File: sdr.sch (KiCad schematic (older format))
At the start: 0 parts

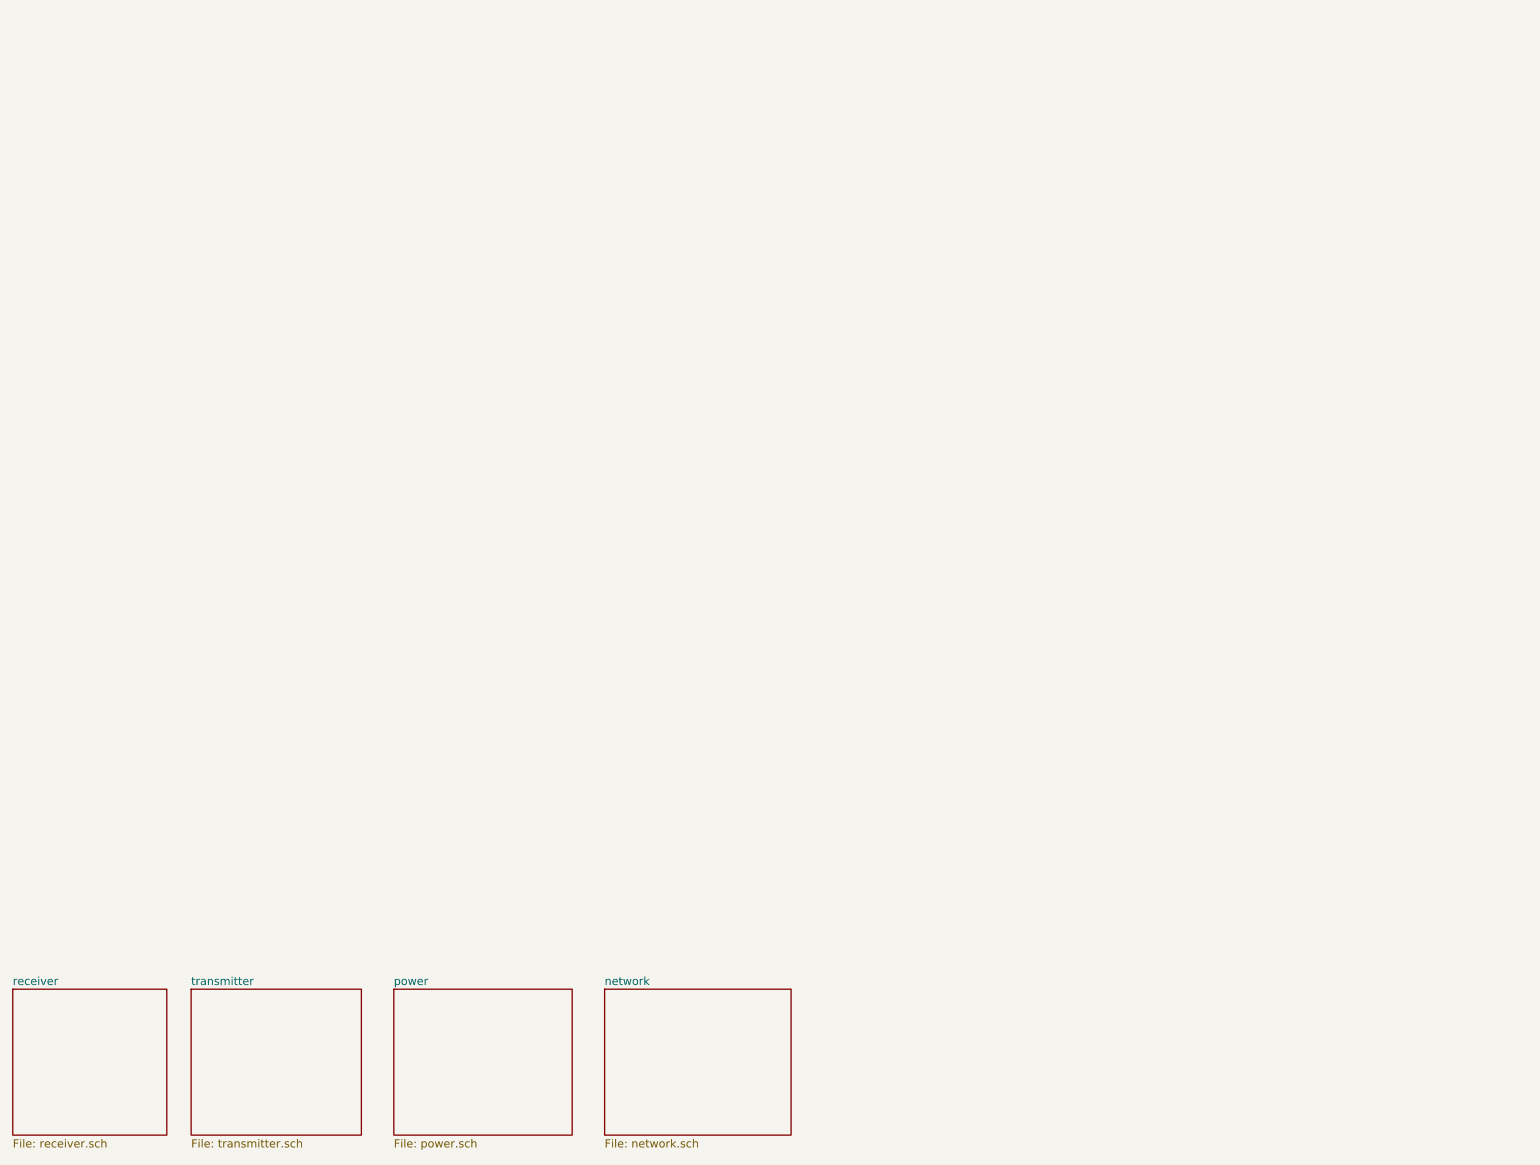
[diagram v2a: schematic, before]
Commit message: work on fpga connections
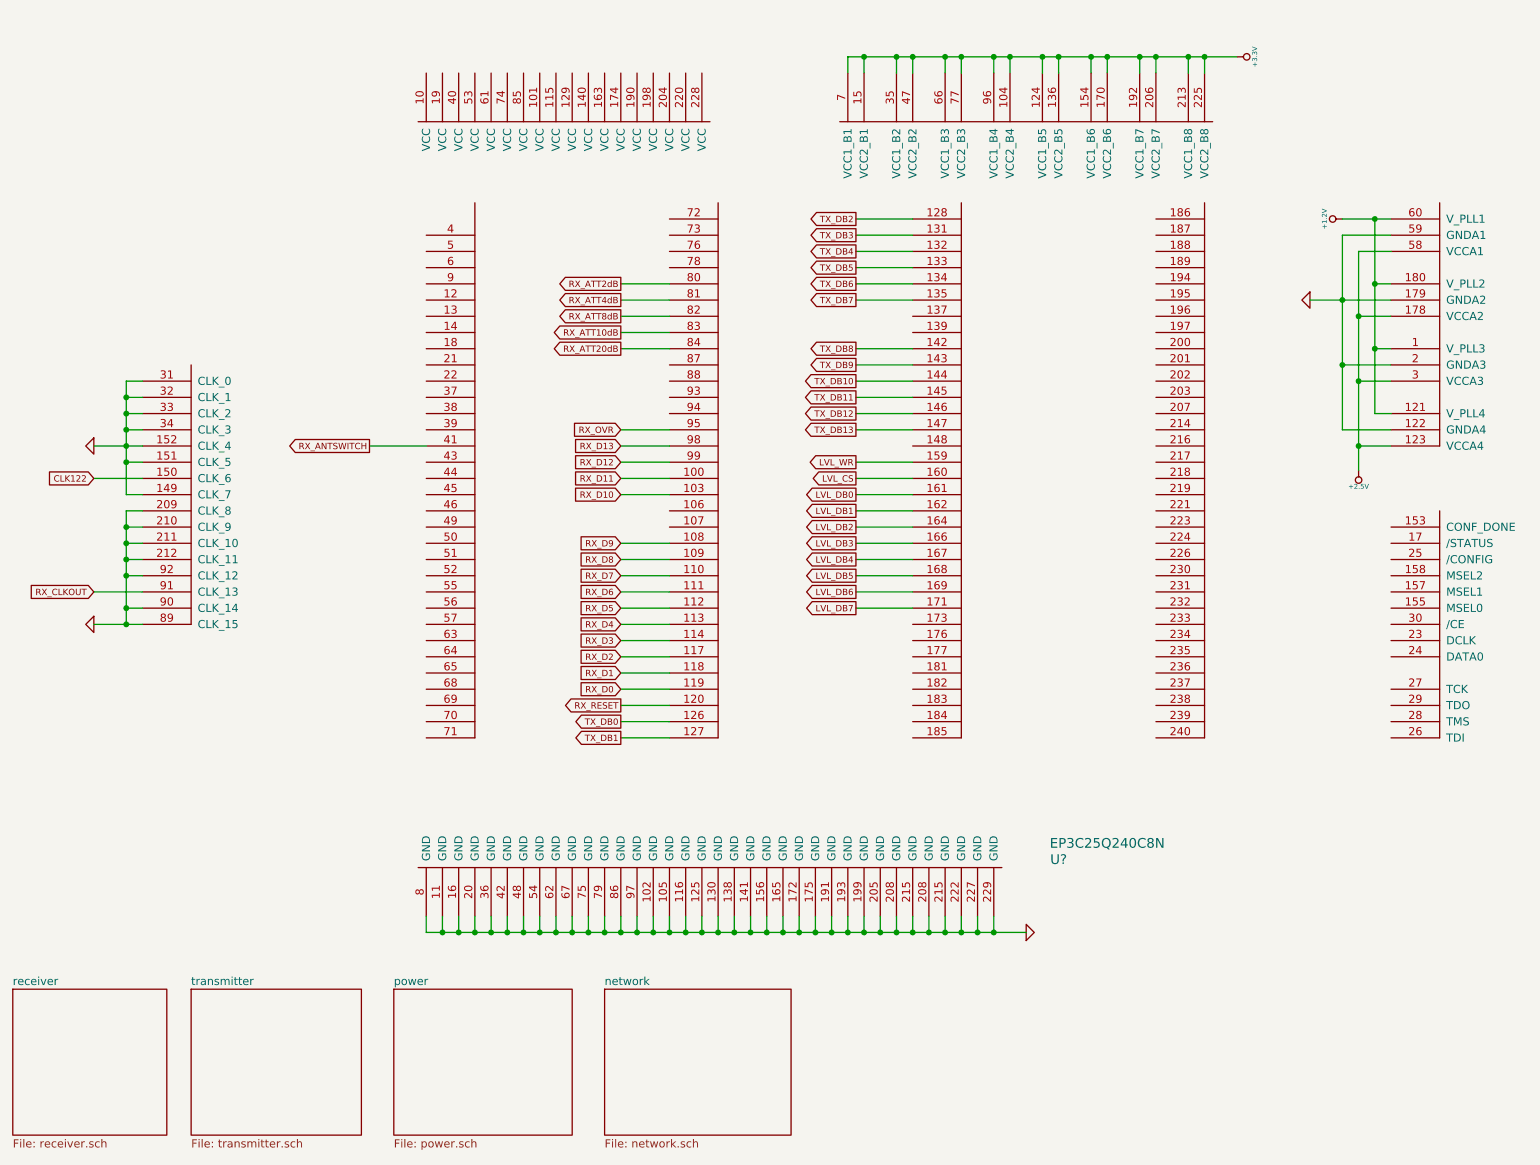
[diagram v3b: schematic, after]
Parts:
- added U?: EP3C25Q240C8N, symbol EP3C25Q240C8N
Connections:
- new net +1.2V: U?.1 (V_PLL3), U?.121 (V_PLL4), U?.180 (V_PLL2), U?.60 (V_PLL1)
- new net +2.5V: U?.123 (VCCA4), U?.178 (VCCA2), U?.3 (VCCA3), U?.58 (VCCA1)
- new net +3.3V: U?.104 (VCC2_B4), U?.124 (VCC1_B5), U?.136 (VCC2_B5), U?.15 (VCC2_B1), U?.154 (VCC1_B6), U?.170 (VCC2_B6), U?.192 (VCC1_B7), U?.206 (VCC2_B7), U?.213 (VCC1_B8), U?.225 (VCC2_B8), U?.35 (VCC1_B2), U?.47 (VCC2_B2), U?.66 (VCC1_B3), U?.7 (VCC1_B1), U?.77 (VCC2_B3), U?.96 (VCC1_B4)
- new net CLK122: U?.150 (CLK_6)
- new net GND: U?.102 (GND), U?.105 (GND), U?.11 (GND), U?.116 (GND), U?.122 (GNDA4), U?.125 (GND), U?.130 (GND), U?.138 (GND), U?.141 (GND), U?.149 (CLK_7), U?.151 (CLK_5), U?.152 (CLK_4), U?.156 (GND), U?.16 (GND), U?.165 (GND), U?.172 (GND), U?.175 (GND), U?.179 (GNDA2), U?.191 (GND), U?.193 (GND), U?.199 (GND), U?.2 (GNDA3), U?.20 (GND), U?.205 (GND), U?.208 (GND), U?.209 (CLK_8), U?.210 (CLK_9), U?.211 (CLK_10), U?.212 (CLK_11), U?.215 (GND), U?.222 (GND), U?.227 (GND), U?.229 (GND), U?.31 (CLK_0), U?.32 (CLK_1), U?.33 (CLK_2), U?.34 (CLK_3), U?.36 (GND), U?.42 (GND), U?.48 (GND), U?.54 (GND), U?.59 (GNDA1), U?.62 (GND), U?.67 (GND), U?.75 (GND), U?.79 (GND), U?.8 (GND), U?.86 (GND), U?.89 (CLK_15), U?.90 (CLK_14), U?.92 (CLK_12), U?.97 (GND)
- new net LVL_CS: U?.160
- new net LVL_DB0: U?.161
- new net LVL_DB1: U?.162
- new net LVL_DB2: U?.164
- new net LVL_DB3: U?.166
- new net LVL_DB4: U?.167
- new net LVL_DB5: U?.168
- new net LVL_DB6: U?.169
- new net LVL_DB7: U?.171
- new net LVL_WR: U?.159
- new net RX_ANTSWITCH: U?.41
- new net RX_ATT10dB: U?.83
- new net RX_ATT20dB: U?.84
- new net RX_ATT2dB: U?.80
- new net RX_ATT4dB: U?.81
- new net RX_ATT8dB: U?.82
- new net RX_CLKOUT: U?.91 (CLK_13)
- new net RX_D0: U?.119
- new net RX_D1: U?.118
- new net RX_D10: U?.103
- new net RX_D11: U?.100
- new net RX_D12: U?.99
- new net RX_D13: U?.98
- new net RX_D2: U?.117
- new net RX_D3: U?.114
- new net RX_D4: U?.113
- new net RX_D5: U?.112
- new net RX_D6: U?.111
- new net RX_D7: U?.110
- new net RX_D8: U?.109
- new net RX_D9: U?.108
- new net RX_OVR: U?.95
- new net RX_RESET: U?.120
- new net TX_DB0: U?.126
- new net TX_DB1: U?.127
- new net TX_DB10: U?.144
- new net TX_DB11: U?.145
- new net TX_DB12: U?.146
- new net TX_DB13: U?.147
- new net TX_DB2: U?.128
- new net TX_DB3: U?.131
- new net TX_DB4: U?.132
- new net TX_DB5: U?.133
- new net TX_DB6: U?.134
- new net TX_DB7: U?.135
- new net TX_DB8: U?.142
- new net TX_DB9: U?.143

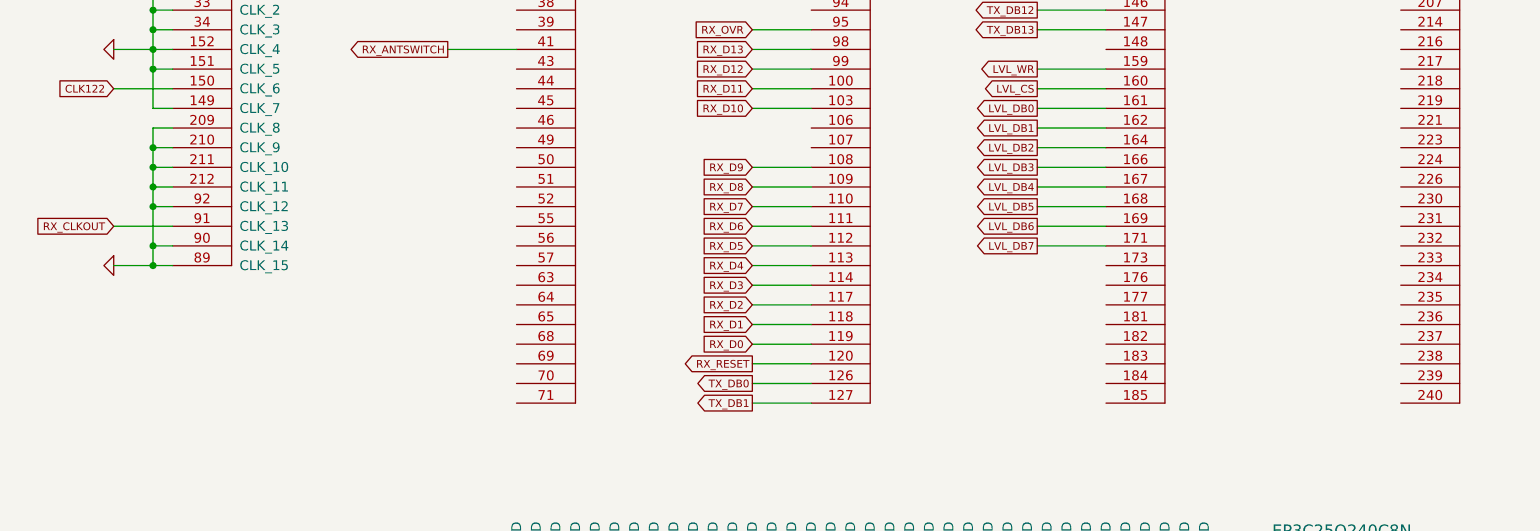
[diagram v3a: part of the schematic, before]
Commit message: some work on the network section
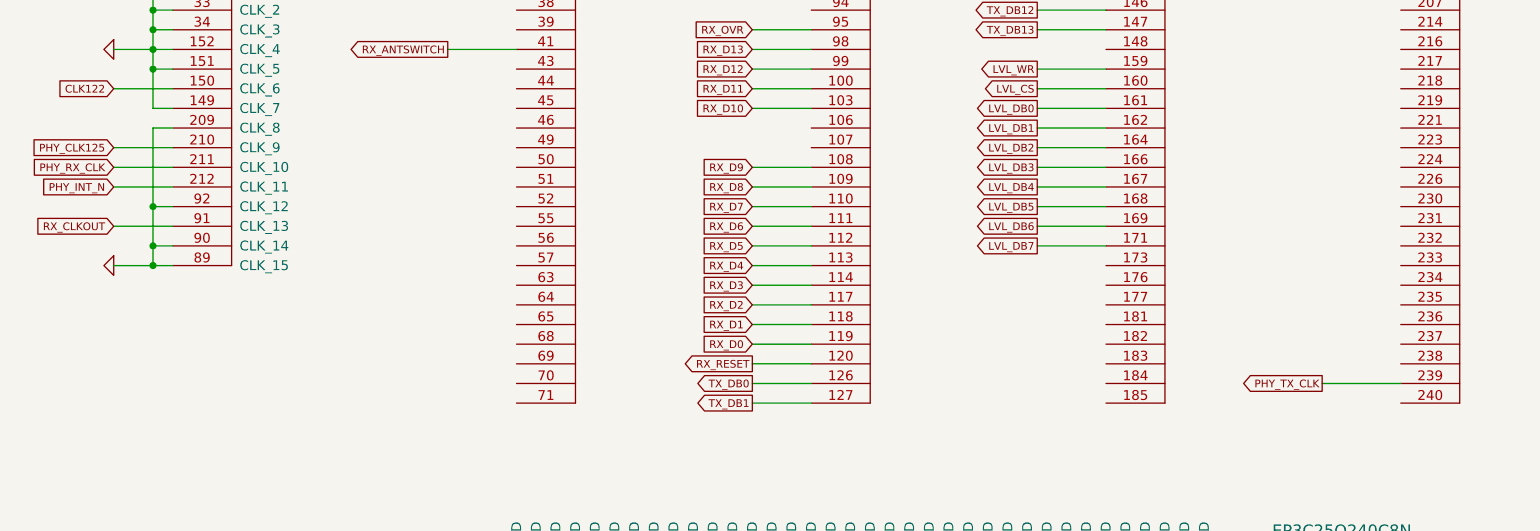
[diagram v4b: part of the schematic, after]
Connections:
- net GND: no longer U?.210 (CLK_9), U?.211 (CLK_10), U?.212 (CLK_11)
- net PHY_TX_CLK: now reaches U?.239
- new net PHY_CLK125: U?.210 (CLK_9)
- new net PHY_INT_N: U?.212 (CLK_11)
- new net PHY_RX_CLK: U?.211 (CLK_10)

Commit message: additions and fixes
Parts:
- added R?: R, symbol R
- added U?: EPCS16, symbol EPCS16
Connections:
- net +1.2V: now also U?.10 (VCC), U?.101 (VCC), U?.115 (VCC), U?.129 (VCC), U?.140 (VCC), U?.163 (VCC), U?.174 (VCC), U?.19 (VCC), U?.190 (VCC), U?.198 (VCC), U?.204 (VCC), U?.220 (VCC), U?.228 (VCC), U?.40 (VCC), U?.53 (VCC), U?.61 (VCC), U?.74 (VCC), U?.85 (VCC)
- net +3.3V: now also U?.157 (MSEL1), U?.3 (VCC), U?.7 (VCC), U?.8 (VCC)
- net GND: now also U?.155 (MSEL0), U?.158 (MSEL2), U?.~ (GND)
- net ASDI: now reaches U?.12
- net ASDI: now also U?.5 (ASDI)
- net NCS: now reaches U?.14
- net NCS: now also U?.1 (NCS)
- net at U?.23 (DCLK): now also U?.6 (DCLK)
- net at U?.24 (DATA0): now also R?.1
- new net: R?.2, U?.2 (DATA)
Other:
- note added: "Main FPGA"

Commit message: fixes
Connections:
- net GND: no longer U?.209 (CLK_8)
- new net CLK_25MHZ: U?.209 (CLK_8)
